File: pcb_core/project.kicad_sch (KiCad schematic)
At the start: 38 parts, among them IC1 TCA9548APWR

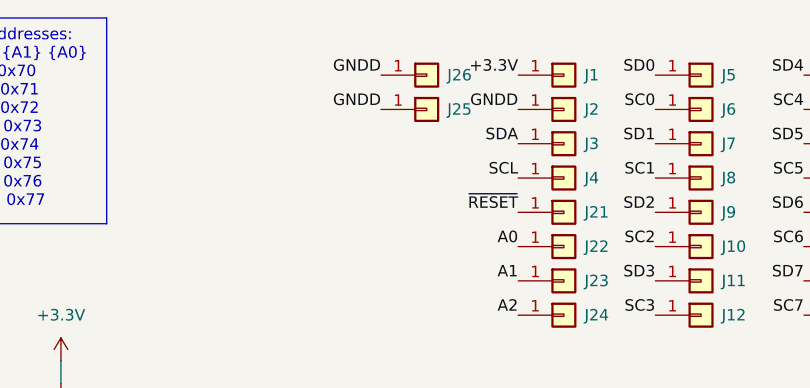
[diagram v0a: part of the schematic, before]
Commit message: Remove connector on own side
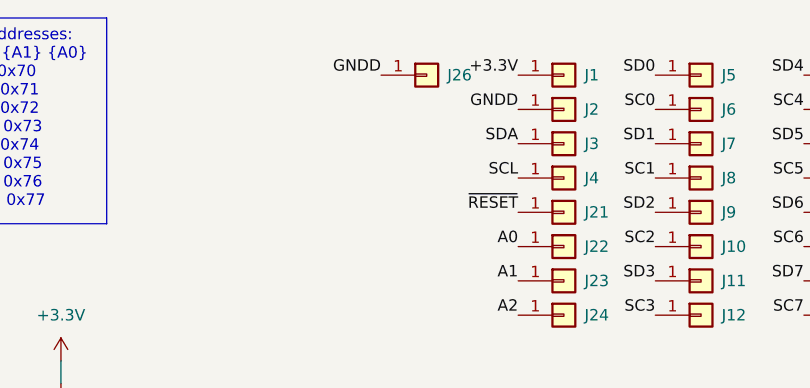
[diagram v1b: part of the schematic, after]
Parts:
- removed J25: ~, Castellated_Holes:Castellated_Hole02, symbol Connector_Generic:Conn_01x01
- J1, J10, J11, J12, J13, J14, J15, J16, J17, J18, J19, J2, J20, J21, J22, J26, J3, J4, J5, J6, J7, J8, J9: now left out of the parts list
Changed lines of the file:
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@@
 		)
 	)
-	(label "GNDD"
-		(at 166.37 26.67 180)
-		(fields_autoplaced yes)
-		(effects
-			(font
-				(size 1.27 1.27)
-			)
-			(justify right bottom)
-		)
-	)
 	(label "A1"
 		(at 181.61 45.72 180)
@@
 		(unit 1)
 		(exclude_from_sim no)
-		(in_bom yes)
+		(in_bom no)
 		(on_board yes)
 		(dnp no)
@@
 		(unit 1)
 		(exclude_from_sim no)
-		(in_bom yes)
+		(in_bom no)
 		(on_board yes)
 		(dnp no)
@@
 		(unit 1)
 		(exclude_from_sim no)
-		(in_bom yes)
+		(in_bom no)
 		(on_board yes)
 		(dnp no)
@@
 		(unit 1)
 		(exclude_from_sim no)
-		(in_bom yes)
+		(in_bom no)
 		(on_board yes)
 		(dnp no)
@@
 		(unit 1)
 		(exclude_from_sim no)
-		(in_bom yes)
+		(in_bom no)
 		(on_board yes)
 		(dnp no)
@@
 		(unit 1)
 		(exclude_from_sim no)
-		(in_bom yes)
+		(in_bom no)
 		(on_board yes)
 		(dnp no)
@@
 		(exclude_from_sim no)
 		(in_bom yes)
-		(on_board yes)
+		(on_board no)
 		(dnp no)
 		(property "Reference" "J24"
@@
 		(unit 1)
 		(exclude_from_sim no)
-		(in_bom yes)
+		(in_bom no)
 		(on_board yes)
 		(dnp no)
@@
 		(unit 1)
 		(exclude_from_sim no)
-		(in_bom yes)
+		(in_bom no)
 		(on_board yes)
 		(dnp no)
@@
 	(symbol
 		(lib_id "Connector_Generic:Conn_01x01")
-		(at 171.45 26.67 0)
-		(unit 1)
-		(exclude_from_sim no)
-		(in_bom yes)
-		(on_board yes)
-		(dnp no)
-		(property "Reference" "J25"
-			(at 173.736 26.67 0)
-			(effects
-				(font
-					(size 1.27 1.27)
-				)
-				(justify left)
-			)
-		)
-		(property "Value" "~"
-			(at 173.99 27.9399 0)
-			(effects
-				(font
-					(size 1.27 1.27)
-				)
-				(justify left)
-			)
-		)
-		(property "Footprint" "Castellated_Holes:Castellated_Hole02"
-			(at 171.45 26.67 0)
-			(effects
-				(font
-					(size 1.27 1.27)
-				)
-				(hide yes)
-			)
-		)
-		(property "Datasheet" "~"
-			(at 171.45 26.67 0)
-			(effects
-				(font
-					(size 1.27 1.27)
-				)
-				(hide yes)
-			)
-		)
-		(property "Description" "Generic connector, single row, 01x01, script generated (kicad-library-utils/schlib/autogen/connector/)"
-			(at 171.45 26.67 0)
-			(effects
-				(font
-					(size 1.27 1.27)
-				)
-				(hide yes)
-			)
-		)
-		(pin "1"
-		)
-		(instances
-			(project "project"
-				(path "/7e72c431-6e21-4045-b5d6-5b8e8920d61f"
-					(reference "J25")
-					(unit 1)
-				)
-			)
-		)
-	)
-	(symbol
-		(lib_id "Connector_Generic:Conn_01x01")
 		(at 186.69 38.1 0)
 		(unit 1)
 		(exclude_from_sim no)
-		(in_bom yes)
+		(in_bom no)
 		(on_board yes)
 		(dnp no)
@@
 		(unit 1)
 		(exclude_from_sim no)
-		(in_bom yes)
+		(in_bom no)
 		(on_board yes)
 		(dnp no)
@@
 		(unit 1)
 		(exclude_from_sim no)
-		(in_bom yes)
+		(in_bom no)
 		(on_board yes)
 		(dnp no)
@@
 		(unit 1)
 		(exclude_from_sim no)
-		(in_bom yes)
+		(in_bom no)
 		(on_board yes)
 		(dnp no)
@@
 		(unit 1)
 		(exclude_from_sim no)
-		(in_bom yes)
+		(in_bom no)
 		(on_board yes)
 		(dnp no)
@@
 		(unit 1)
 		(exclude_from_sim no)
-		(in_bom yes)
+		(in_bom no)
 		(on_board yes)
 		(dnp no)
@@
 		(unit 1)
 		(exclude_from_sim no)
-		(in_bom yes)
+		(in_bom no)
 		(on_board yes)
 		(dnp no)
@@
 		(unit 1)
 		(exclude_from_sim no)
-		(in_bom yes)
+		(in_bom no)
 		(on_board yes)
 		(dnp no)
@@
 		(unit 1)
 		(exclude_from_sim no)
-		(in_bom yes)
+		(in_bom no)
 		(on_board yes)
 		(dnp no)
@@
 		(unit 1)
 		(exclude_from_sim no)
-		(in_bom yes)
+		(in_bom no)
 		(on_board yes)
 		(dnp no)
@@
 		(unit 1)
 		(exclude_from_sim no)
-		(in_bom yes)
+		(in_bom no)
 		(on_board yes)
 		(dnp no)
@@
 		(unit 1)
 		(exclude_from_sim no)
-		(in_bom yes)
+		(in_bom no)
 		(on_board yes)
 		(dnp no)
@@
 		(exclude_from_sim no)
 		(in_bom yes)
-		(on_board yes)
+		(on_board no)
 		(dnp no)
 		(property "Reference" "J23"
@@
 		(unit 1)
 		(exclude_from_sim no)
-		(in_bom yes)
+		(in_bom no)
 		(on_board yes)
 		(dnp no)
@@
 		(unit 1)
 		(exclude_from_sim no)
-		(in_bom yes)
+		(in_bom no)
 		(on_board yes)
 		(dnp no)
@@
 		(unit 1)
 		(exclude_from_sim no)
-		(in_bom yes)
+		(in_bom no)
 		(on_board yes)
 		(dnp no)
